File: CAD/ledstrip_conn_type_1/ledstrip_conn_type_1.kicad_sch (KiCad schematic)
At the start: 3 parts, among them J1 led_strip_output, J2 led_strip_input, J3 led_strip_input

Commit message: Feat: Library mess fixed
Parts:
- J1: footprint led_strip_lib:strip_print_output -> ledstrip_footprints:strip_print_output
- J2, J3: footprint led_strip_lib:strip_print_input -> ledstrip_footprints:strip_print_input
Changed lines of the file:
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@@
     (property "Reference" "J3" (id 0) (at 171.8445 69.85 0))
     (property "Value" "led_strip_input" (id 1) (at 171.8445 72.39 0))
-    (property "Footprint" "led_strip_lib:strip_print_input" (id 2) (at 161.29 73.66 0)
+    (property "Footprint" "ledstrip_footprints:strip_print_input" (id 2) (at 161.29 73.66 0)
       (effects (font (size 1.27 1.27)) hide)
     )
@@
     (pin "3")
   )
-  (symbol (lib_id "led_strip_lib:led_strip_input") (at 137.16 91.44 270) (unit 1)
+  (symbol (lib_name "led_strip_input_1") (lib_id "led_strip_lib:led_strip_input") (at 137.16 91.44 270) (unit 1)
     (in_bom yes) (on_board yes) (fields_autoplaced)
     (property "Reference" "J2" (id 0) (at 138.43 115.9644 90)
@@
       (effects (font (size 1.27 1.27)) (justify left))
     )
-    (property "Footprint" "led_strip_lib:strip_print_input" (id 2) (at 138.43 106.68 0)
+    (property "Footprint" "ledstrip_footprints:strip_print_input" (id 2) (at 138.43 106.68 0)
       (effects (font (size 1.27 1.27)) hide)
     )
@@
     (property "Reference" "J1" (id 0) (at 94.7984 69.85 0))
     (property "Value" "led_strip_output" (id 1) (at 94.7984 72.39 0))
-    (property "Footprint" "led_strip_lib:strip_print_output" (id 2) (at 85.09 73.66 0)
+    (property "Footprint" "ledstrip_footprints:strip_print_output" (id 2) (at 85.09 73.66 0)
       (effects (font (size 1.27 1.27)) hide)
     )
@@
   (symbol_instances
     (path "/cdeee8db-b57e-4fd9-9652-480b2e77c2e7"
-      (reference "J1") (unit 1) (value "led_strip_output") (footprint "led_strip_lib:strip_print_output")
+      (reference "J1") (unit 1) (value "led_strip_output") (footprint "ledstrip_footprints:strip_print_output")
     )
     (path "/bdf056b6-c44f-4e21-94f9-894ae4baa5f3"
-      (reference "J2") (unit 1) (value "led_strip_input") (footprint "led_strip_lib:strip_print_input")
+      (reference "J2") (unit 1) (value "led_strip_input") (footprint "ledstrip_footprints:strip_print_input")
     )
     (path "/3ba65869-b2ea-4ed4-b940-eb7161ee6530"
-      (reference "J3") (unit 1) (value "led_strip_input") (footprint "led_strip_lib:strip_print_input")
+      (reference "J3") (unit 1) (value "led_strip_input") (footprint "ledstrip_footprints:strip_print_input")
     )
   )

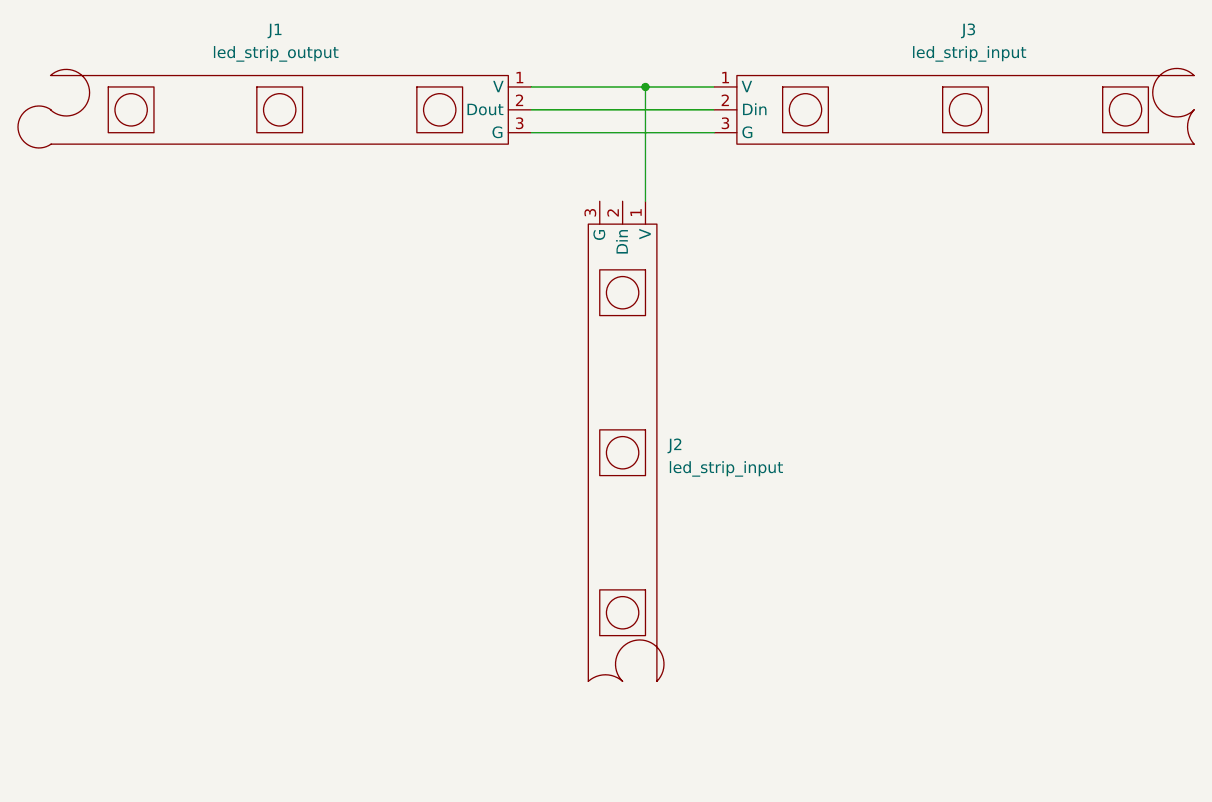
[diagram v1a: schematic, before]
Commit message: fix: direction of ledstrips
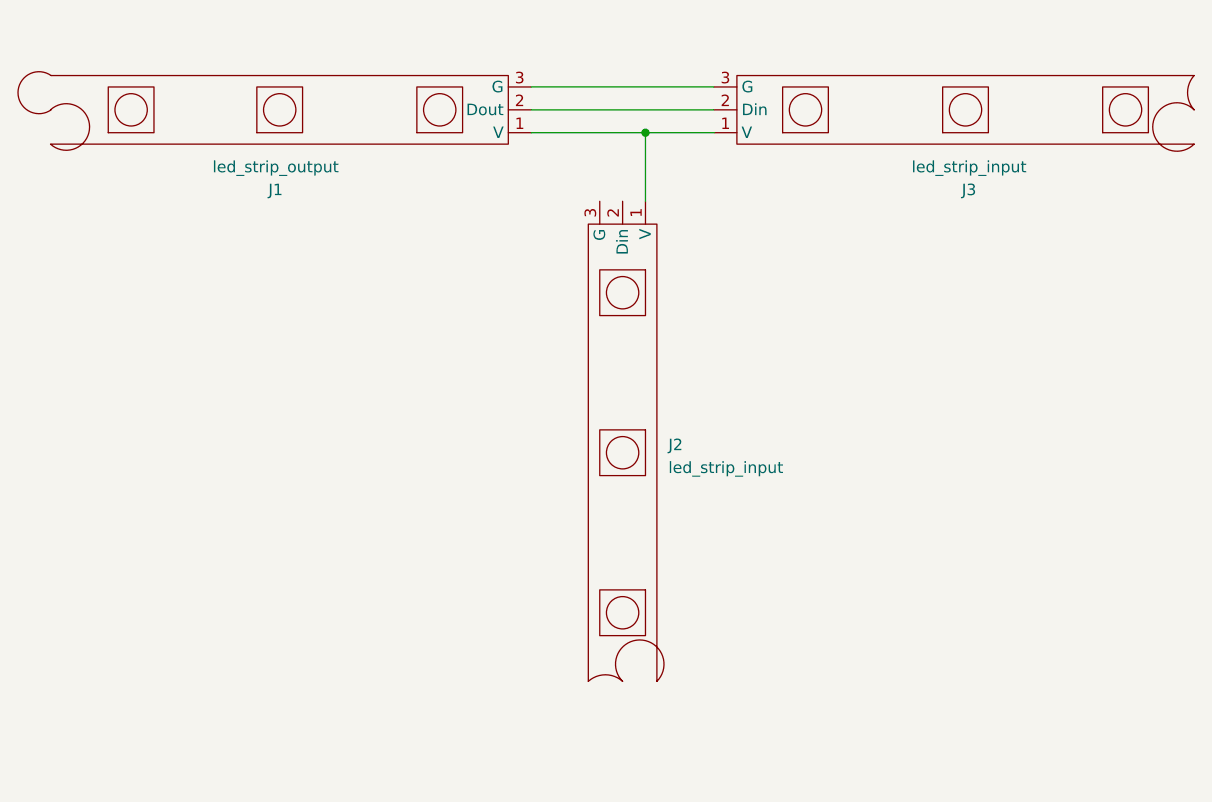
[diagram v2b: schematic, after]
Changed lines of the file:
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@@
 (kicad_sch (version 20211123) (generator eeschema)
   (paper "A4")
-  (junction (at 135.89 76.2) (diameter 0) (color 0 0 0 0)
+  (junction (at 135.89 81.28) (diameter 0) (color 0 0 0 0)
   )
-  (wire (pts (xy 135.89 76.2) (xy 143.51 76.2))
+  (wire (pts (xy 135.89 81.28) (xy 143.51 81.28))
     (stroke (width 0) (type default) (color 0 0 0 0))
   )
@@
     (stroke (width 0) (type default) (color 0 0 0 0))
   )
-  (wire (pts (xy 135.89 76.2) (xy 135.89 88.9))
+  (wire (pts (xy 123.19 76.2) (xy 143.51 76.2))
     (stroke (width 0) (type default) (color 0 0 0 0))
   )
-  (wire (pts (xy 123.19 76.2) (xy 135.89 76.2))
+  (wire (pts (xy 123.19 81.28) (xy 135.89 81.28))
     (stroke (width 0) (type default) (color 0 0 0 0))
   )
-  (wire (pts (xy 123.19 81.28) (xy 143.51 81.28))
+  (wire (pts (xy 135.89 81.28) (xy 135.89 88.9))
     (stroke (width 0) (type default) (color 0 0 0 0))
   )
-  (symbol (lib_id "led_strip_lib:led_strip_input") (at 146.05 74.93 0) (unit 1)
+  (symbol (lib_id "led_strip_lib:led_strip_input") (at 146.05 82.55 0) (mirror x) (unit 1)
     (in_bom yes) (on_board yes) (fields_autoplaced)
-    (property "Reference" "J3" (id 0) (at 171.8445 69.85 0))
-    (property "Value" "led_strip_input" (id 1) (at 171.8445 72.39 0))
-    (property "Footprint" "ledstrip_footprints:strip_print_input" (id 2) (at 161.29 73.66 0)
+    (property "Reference" "J3" (id 0) (at 171.8445 87.63 0))
+    (property "Value" "led_strip_input" (id 1) (at 171.8445 85.09 0))
+    (property "Footprint" "ledstrip_footprints:strip_print_input" (id 2) (at 161.29 83.82 0)
       (effects (font (size 1.27 1.27)) hide)
     )
-    (property "Datasheet" "" (id 3) (at 146.05 74.93 0)
+    (property "Datasheet" "" (id 3) (at 146.05 82.55 0)
       (effects (font (size 1.27 1.27)) hide)
     )
@@
     (pin "3")
   )
-  (symbol (lib_id "led_strip_lib:led_strip_output") (at 69.85 74.93 0) (unit 1)
+  (symbol (lib_id "led_strip_lib:led_strip_output") (at 69.85 82.55 0) (mirror x) (unit 1)
     (in_bom yes) (on_board yes) (fields_autoplaced)
-    (property "Reference" "J1" (id 0) (at 94.7984 69.85 0))
-    (property "Value" "led_strip_output" (id 1) (at 94.7984 72.39 0))
-    (property "Footprint" "ledstrip_footprints:strip_print_output" (id 2) (at 85.09 73.66 0)
+    (property "Reference" "J1" (id 0) (at 94.7984 87.63 0))
+    (property "Value" "led_strip_output" (id 1) (at 94.7984 85.09 0))
+    (property "Footprint" "ledstrip_footprints:strip_print_output" (id 2) (at 85.09 83.82 0)
       (effects (font (size 1.27 1.27)) hide)
     )
-    (property "Datasheet" "" (id 3) (at 69.85 74.93 0)
+    (property "Datasheet" "" (id 3) (at 69.85 82.55 0)
       (effects (font (size 1.27 1.27)) hide)
     )

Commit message: Feat: New design, single connector
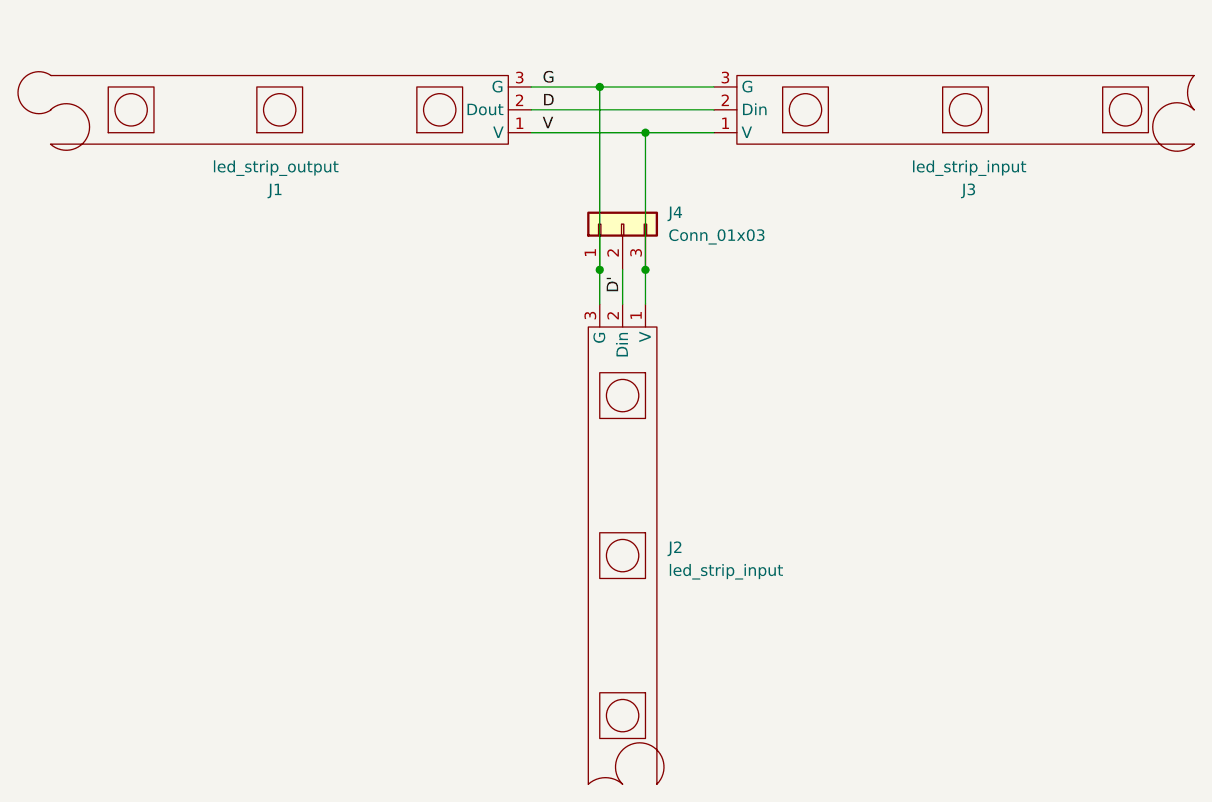
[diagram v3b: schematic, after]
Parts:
- added J4: Conn_01x03, Connector_PinHeader_2.54mm:PinHeader_1x03_P2.54mm_Vertical, symbol Connector_Generic:Conn_01x03
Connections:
- net V: now reaches J1.1 (V), J2.1 (V), J3.1 (V)
- net V: now also J4.3 (Pin_3)
- net D: now reaches J1.2 (Dout), J3.2 (Din)
- net G: now reaches J1.3 (G), J3.3 (G)
- net G: now also J2.3 (G), J4.1 (Pin_1)
- net D': now reaches J2.2 (Din)
- net D': now also J4.2 (Pin_2)
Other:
- moved on the sheet: J2
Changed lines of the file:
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@@
   (junction (at 135.89 81.28) (diameter 0) (color 0 0 0 0)
   )
+  (junction (at 130.81 76.2) (diameter 0) (color 0 0 0 0)
+  )
+  (junction (at 130.81 96.52) (diameter 0) (color 0 0 0 0)
+  )
+  (junction (at 135.89 96.52) (diameter 0) (color 0 0 0 0)
+  )
   (wire (pts (xy 135.89 81.28) (xy 143.51 81.28))
+    (stroke (width 0) (type default) (color 0 0 0 0))
+  )
+  (wire (pts (xy 130.81 76.2) (xy 130.81 96.52))
     (stroke (width 0) (type default) (color 0 0 0 0))
   )
@@
     (stroke (width 0) (type default) (color 0 0 0 0))
   )
-  (wire (pts (xy 123.19 76.2) (xy 143.51 76.2))
+  (wire (pts (xy 135.89 96.52) (xy 135.89 100.33))
+    (stroke (width 0) (type default) (color 0 0 0 0))
+  )
+  (wire (pts (xy 123.19 76.2) (xy 130.81 76.2))
     (stroke (width 0) (type default) (color 0 0 0 0))
   )
@@
     (stroke (width 0) (type default) (color 0 0 0 0))
   )
-  (wire (pts (xy 135.89 81.28) (xy 135.89 88.9))
+  (wire (pts (xy 130.81 96.52) (xy 130.81 100.33))
     (stroke (width 0) (type default) (color 0 0 0 0))
+  )
+  (wire (pts (xy 130.81 76.2) (xy 143.51 76.2))
+    (stroke (width 0) (type default) (color 0 0 0 0))
+  )
+  (wire (pts (xy 135.89 81.28) (xy 135.89 96.52))
+    (stroke (width 0) (type default) (color 0 0 0 0))
+  )
+  (wire (pts (xy 133.35 96.52) (xy 133.35 100.33))
+    (stroke (width 0) (type default) (color 0 0 0 0))
+  )
+  (label "D'" (at 133.35 99.06 90)
+    (effects (font (size 1.27 1.27)) (justify left bottom))
+  )
+  (label "V" (at 124.46 81.28 0)
+    (effects (font (size 1.27 1.27)) (justify left bottom))
+  )
+  (label "D" (at 124.46 78.74 0)
+    (effects (font (size 1.27 1.27)) (justify left bottom))
+  )
+  (label "G" (at 124.46 76.2 0)
+    (effects (font (size 1.27 1.27)) (justify left bottom))
+  )
+  (symbol (lib_id "Connector_Generic:Conn_01x03") (at 133.35 91.44 90) (unit 1)
+    (in_bom yes) (on_board yes) (fields_autoplaced)
+    (property "Reference" "J4" (id 0) (at 138.43 90.1699 90)
+      (effects (font (size 1.27 1.27)) (justify right))
+    )
+    (property "Value" "Conn_01x03" (id 1) (at 138.43 92.7099 90)
+      (effects (font (size 1.27 1.27)) (justify right))
+    )
+    (property "Footprint" "Connector_PinHeader_2.54mm:PinHeader_1x03_P2.54mm_Vertical" (id 2) (at 133.35 91.44 0)
+      (effects (font (size 1.27 1.27)) hide)
+    )
+    (property "Datasheet" "~" (id 3) (at 133.35 91.44 0)
+      (effects (font (size 1.27 1.27)) hide)
+    )
+    (pin "1")
+    (pin "2")
+    (pin "3")
   )
   (symbol (lib_id "led_strip_lib:led_strip_input") (at 146.05 82.55 0) (mirror x) (unit 1)
@@
     (pin "3")
   )
-  (symbol (lib_name "led_strip_input_1") (lib_id "led_strip_lib:led_strip_input") (at 137.16 91.44 270) (unit 1)
+  (symbol (lib_id "led_strip_lib:led_strip_input") (at 137.16 102.87 270) (unit 1)
     (in_bom yes) (on_board yes) (fields_autoplaced)
-    (property "Reference" "J2" (id 0) (at 138.43 115.9644 90)
+    (property "Reference" "J2" (id 0) (at 138.43 127.3944 90)
       (effects (font (size 1.27 1.27)) (justify left))
     )
-    (property "Value" "led_strip_input" (id 1) (at 138.43 118.5044 90)
+    (property "Value" "led_strip_input" (id 1) (at 138.43 129.9344 90)
       (effects (font (size 1.27 1.27)) (justify left))
     )
-    (property "Footprint" "ledstrip_footprints:strip_print_input" (id 2) (at 138.43 106.68 0)
+    (property "Footprint" "ledstrip_footprints:strip_print_input" (id 2) (at 138.43 118.11 0)
       (effects (font (size 1.27 1.27)) hide)
     )
-    (property "Datasheet" "" (id 3) (at 137.16 91.44 0)
+    (property "Datasheet" "" (id 3) (at 137.16 102.87 0)
       (effects (font (size 1.27 1.27)) hide)
     )
@@
       (reference "J3") (unit 1) (value "led_strip_input") (footprint "ledstrip_footprints:strip_print_input")
     )
+    (path "/2c5cd0ff-af78-4b8f-8637-0ba300890720"
+      (reference "J4") (unit 1) (value "Conn_01x03") (footprint "Connector_PinHeader_2.54mm:PinHeader_1x03_P2.54mm_Vertical")
+    )
   )
